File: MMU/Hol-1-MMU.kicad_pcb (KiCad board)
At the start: 2 copper layers, 106.7 x 76.2 mm, 36 parts, among them P1 DATA BUS, P2 ADDRESS PORT, P3 DATA PORT, P4 MMU CONTROL, P5 Power, SW1 HEX_SWITCH, SW2 HEX_SWITCH, SW3 HEX_SWITCH, SW4 HEX_SWITCH, SW5 DPDT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

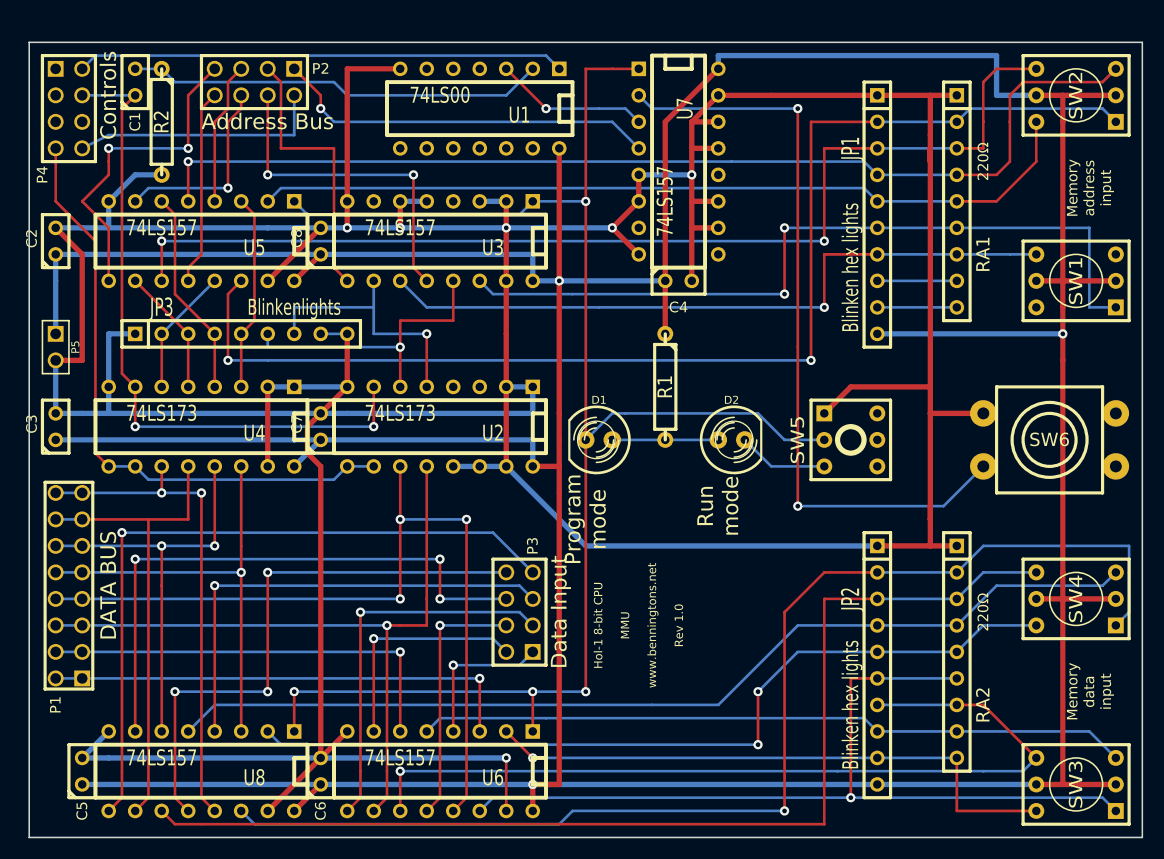
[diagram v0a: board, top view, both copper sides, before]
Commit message: v1.5.10 MMU: better space ICs
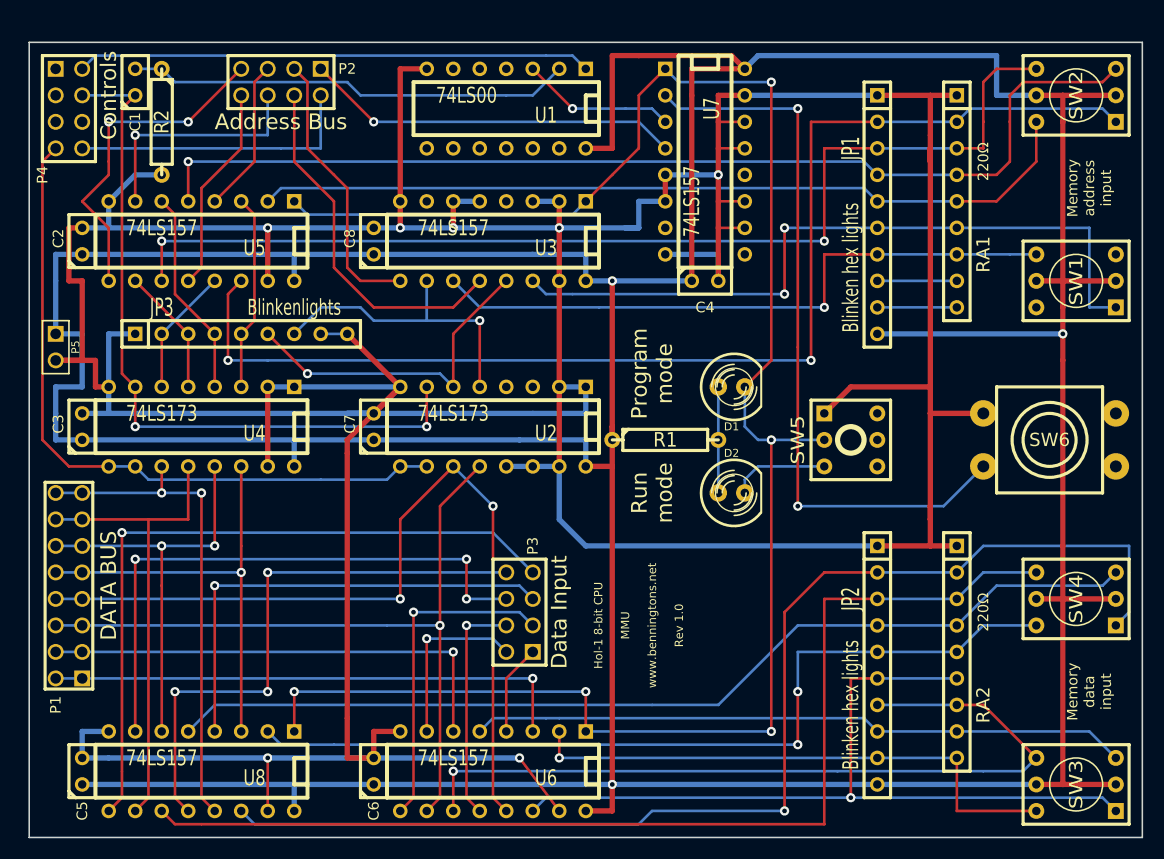
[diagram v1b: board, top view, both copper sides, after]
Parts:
- moved D1 13.7 mm to (171.4, 96.5), turned to 0 degrees
- moved D2 5.08 mm to (171.4, 106.7)
- moved U2 5.08 mm to (148.6, 100.3)
- moved U3 5.08 mm to (148.6, 82.5)
- moved U6 5.08 mm to (148.6, 133.3)
- moved R1 5.08 mm to (165.1, 101.6), turned to 0 degrees
- moved C6 5.08 mm to (137.2, 133.3)
- moved C7 5.08 mm to (137.2, 100.3)
- moved C8 5.08 mm to (137.2, 82.5)
- moved U1 2.54 mm to (149.9, 69.8)
- moved P2 2.54 mm to (128.3, 67.3)
- moved C2 2.54 mm to (109.2, 82.5)
- moved C3 2.54 mm to (109.2, 100.3)
- moved C4 2.54 mm to (168.9, 86.4)
- moved U7 2.54 mm to (168.9, 74.9)
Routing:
- net +5V: track 465.0 -> 492.5 mm
- net GND: track 506.8 -> 534.2 mm, vias 6 -> 7
- net /PROG: track 154.3 -> 179.0 mm, vias 6 -> 7
- net /IN-D: track 59.0 -> 67.4 mm
- net N-0000010: track 14.5 -> 8.67 mm, vias 1 -> 0
- net N-0000046: track 40.6 -> 45.7 mm
- net N-0000045: track 45.7 -> 50.8 mm
- net N-0000040: track 75.5 -> 70.4 mm
- net N-0000021: track 82.6 -> 77.6 mm
- net N-0000011: track 22.1 -> 17.0 mm
- net /CLK: track 64.6 -> 69.6 mm
- net N-0000041: track 67.1 -> 62.0 mm
- net N-0000020: track 83.6 -> 78.5 mm
- net N-0000022: track 68.1 -> 63.1 mm
- net N-0000013: track 36.6 -> 31.5 mm
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
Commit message: v1.5.11 MMU: accommodate larger IDC headers
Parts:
- P1: footprint pin_array_8x2 -> IDC_head_8x2
- P2, P3, P4: footprint pin_array_4x2 -> IDC_head_4x2
- moved C3 3.59 mm to (111.8, 97.8)
- moved C2 2.54 mm to (111.8, 82.5)
- moved C5 2.54 mm to (111.8, 133.3)
- moved JP3 2.54 mm to (127.0, 91.4)
- moved U4 2.54 mm to (123.2, 100.3)
- moved U5 2.54 mm to (123.2, 82.5)
- moved U8 2.54 mm to (123.2, 133.3)
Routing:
- net GND: track 534.2 -> 517.5 mm
- net +5V: track 492.5 -> 480.5 mm
- net N-0000047: track 117.1 -> 109.8 mm, vias 2 -> 1
- net /PROG: track 179.0 -> 174.7 mm
- net N-000006: track 22.9 -> 18.8 mm
- net N-000005: track 32.1 -> 29.3 mm
- net N-0000049: track 101.2 -> 98.6 mm
- net N-0000042: track 46.2 -> 48.8 mm, vias 0 -> 1
- net N-0000056: track 55.1 -> 52.6 mm
- net N-0000053: track 55.9 -> 53.3 mm
- net N-0000044: track 43.2 -> 45.7 mm
- net N-0000054: track 47.5 -> 50.1 mm
- net N-0000052: track 45.0 -> 42.4 mm
- net N-0000048: track 103.4 -> 100.9 mm
- net N-0000039: track 40.6 -> 43.2 mm
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
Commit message: v1.5.12 MMU: accommodate larger JST header
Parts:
- P5: footprint PIN_ARRAY_2X1 -> JST_head_2X1
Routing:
- net +5V: track 480.5 -> 483.4 mm
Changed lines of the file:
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@@
     (links 192)
     (no_connects 0)
-    (area 103.2764 59.706934 210.895001 143.493066)
+    (area 103.733599 58.205512 210.895001 143.493066)
     (thickness 1.6)
     (drawings 13)
@@
   )
   (setup
-    (last_trace_width 0.254)
+    (last_trace_width 0.508)
     (user_trace_width 0.508)
     (trace_clearance 0.254)
@@
     (pcb_text_width 0.3)
     (pcb_text_size 1.5 1.5)
-    (mod_edge_width 0.3048)
+    (mod_edge_width 0.1524)
     (mod_text_size 1 1)
     (mod_text_width 0.15)
@@
     )
   )
-  (module PIN_ARRAY_2X1 (layer F.Cu)
-    (at 106.68 92.71 270)
-    (descr "Connecteurs 2 pins")
-    (tags "CONN DEV")
-    (fp_text reference P5 (at 0 -1.905 270) (layer F.SilkS)
-      (effects (font (size 0.762 0.762) (thickness 0.1524)))
-    )
-    (fp_text value Power (at 0 -1.905 270) (layer F.SilkS) hide
-      (effects (font (size 0.762 0.762) (thickness 0.1524)))
-    )
-    (fp_line (start -2.54 1.27) (end -2.54 -1.27) (layer F.SilkS) (width 0.1524))
-    (fp_line (start -2.54 -1.27) (end 2.54 -1.27) (layer F.SilkS) (width 0.1524))
-    (fp_line (start 2.54 -1.27) (end 2.54 1.27) (layer F.SilkS) (width 0.1524))
-    (fp_line (start 2.54 1.27) (end -2.54 1.27) (layer F.SilkS) (width 0.1524))
-    (pad 1 thru_hole rect (at -1.27 0 270) (size 1.524 1.524) (drill 1.016)
-      (layers *.Cu *.Mask F.SilkS)
-      (net 1 +5V)
-    )
-    (pad 2 thru_hole circle (at 1.27 0 270) (size 1.524 1.524) (drill 1.016)
-      (layers *.Cu *.Mask F.SilkS)
-      (net 8 GND)
-    )
-    (model pin_array/pins_array_2x1.wrl
-      (at (xyz 0 0 0))
-      (scale (xyz 1 1 1))
-      (rotate (xyz 0 0 0))
-    )
-  )
   (module C1 (layer F.Cu)
     (at 111.76 82.55 90)
@@
     )
   )
+  (module JST_head_2X1 (layer F.Cu)
+    (at 106.68 92.71 270)
+    (descr "JST header 2 pins")
+    (tags "CONN JST 2")
+    (fp_text reference P5 (at 0 1.27 270) (layer F.SilkS)
+      (effects (font (size 0.762 0.762) (thickness 0.1524)))
+    )
+    (fp_text value Power (at 0 -1.905 270) (layer F.SilkS)
+      (effects (font (size 0.762 0.762) (thickness 0.1524)))
+    )
+    (fp_line (start 0.635 1.27) (end 2.54 1.27) (layer F.SilkS) (width 0.1524))
+    (fp_line (start -2.54 1.27) (end -0.635 1.27) (layer F.SilkS) (width 0.1524))
+    (fp_line (start -2.54 -1.27) (end -2.54 -2.54) (layer F.SilkS) (width 0.1524))
+    (fp_line (start -2.54 -2.54) (end 2.54 -2.54) (layer F.SilkS) (width 0.1524))
+    (fp_line (start 2.54 -2.54) (end 2.54 -1.27) (layer F.SilkS) (width 0.1524))
+    (fp_line (start -2.54 1.27) (end -2.54 -1.27) (layer F.SilkS) (width 0.1524))
+    (fp_line (start 2.54 -1.27) (end 2.54 1.27) (layer F.SilkS) (width 0.1524))
+    (pad 1 thru_hole rect (at -1.27 0 270) (size 1.524 1.524) (drill 1.016)
+      (layers *.Cu *.Mask F.SilkS)
+      (net 1 +5V)
+    )
+    (pad 2 thru_hole circle (at 1.27 0 270) (size 1.524 1.524) (drill 1.016)
+      (layers *.Cu *.Mask F.SilkS)
+      (net 8 GND)
+    )
+    (model pin_array/pins_array_2x1.wrl
+      (at (xyz 0 0 0))
+      (scale (xyz 1 1 1))
+      (rotate (xyz 0 0 0))
+    )
+  )
   (gr_text "Program\nmode" (at 163.83 95.25 90) (layer F.SilkS)
     (effects (font (size 1.5 1.5) (thickness 0.3)))
@@
   (gr_line (start 104.14 139.7) (end 210.82 139.7) (angle 90) (layer Edge.Cuts) (width 0.15))
   (gr_line (start 104.14 63.5) (end 104.14 139.7) (angle 90) (layer Edge.Cuts) (width 0.15))
+  (segment (start 106.68 91.44) (end 106.68 83.82) (width 0.508) (layer B.Cu) (net 1) (status 400000))
+  (segment (start 106.68 83.82) (end 111.76 83.82) (width 0.508) (layer B.Cu) (net 1) (status 800000))
   (segment (start 111.76 99.06) (end 114.3 101.6) (width 0.508) (layer B.Cu) (net 1))
   (segment (start 114.3 101.6) (end 132.08 101.6) (width 0.508) (layer B.Cu) (net 1))
   (segment (start 111.76 83.82) (end 132.08 83.82) (width 0.508) (layer B.Cu) (net 1))
-  (segment (start 106.68 91.44) (end 111.76 86.36) (width 0.508) (layer B.Cu) (net 1))
-  (segment (start 111.76 86.36) (end 111.76 83.82) (width 0.508) (layer B.Cu) (net 1))
   (segment (start 132.08 86.36) (end 132.08 83.82) (width 0.508) (layer B.Cu) (net 1))
   (segment (start 111.76 99.06) (end 109.22 99.06) (width 0.508) (layer B.Cu) (net 1))

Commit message: v1.5.13 MMU: adjustments during construction
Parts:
- C3: footprint C1 -> C2
- moved C3 1.27 mm to (111.8, 99.1)
- turned SW5 to 90 degrees
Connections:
- SW6 pad 1: GND -> N-0000057
- SW6 pad 2: N-0000057 -> GND
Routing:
- net /PROG: track 174.7 -> 190.2 mm, vias 7 -> 6
- net N-0000057: track 70.7 -> 56.5 mm
- net GND: track 517.5 -> 508.8 mm
- net N-000009: track 9.42 -> 18.1 mm
- net +5V: track 483.4 -> 484.5 mm, vias 3 -> 6
- net /IN-D: track 66.7 -> 67.4 mm

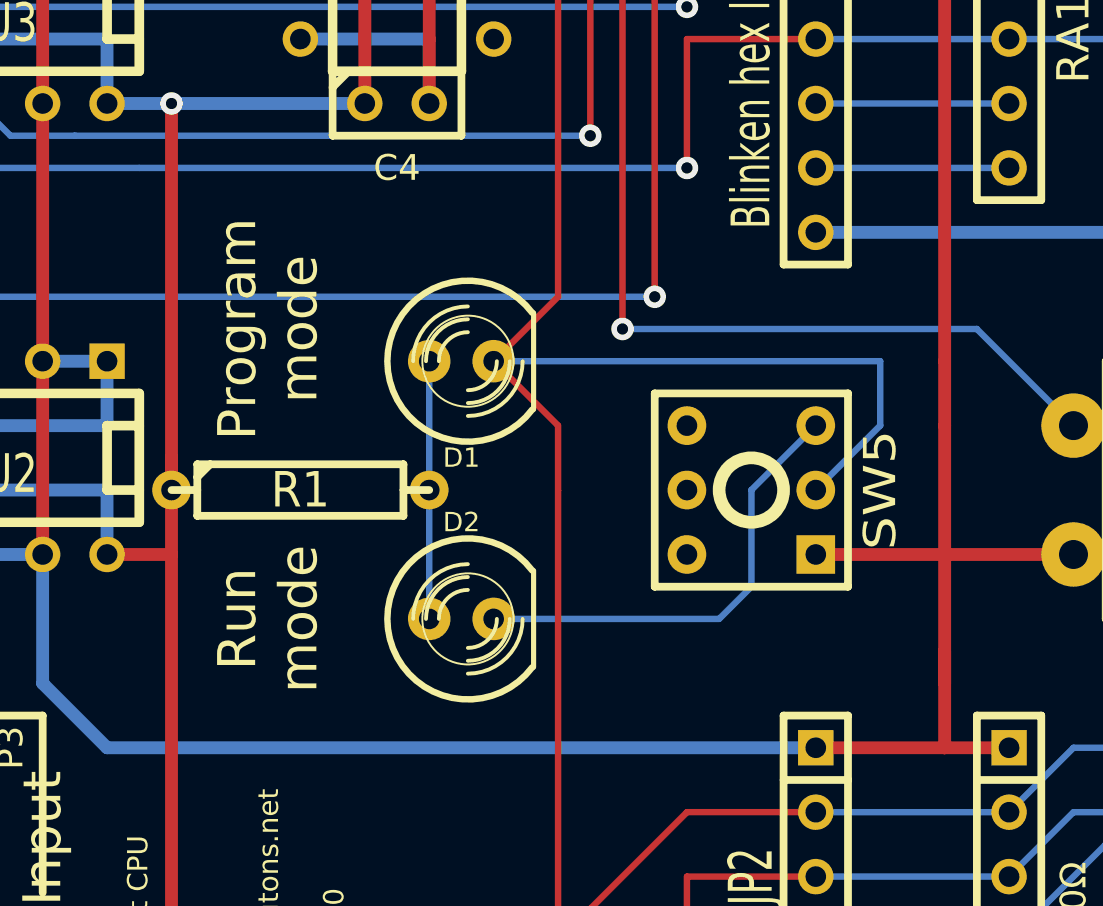
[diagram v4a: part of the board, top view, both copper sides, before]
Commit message: v1.5.16 MMU: don't share a resistor between program and run LEDs
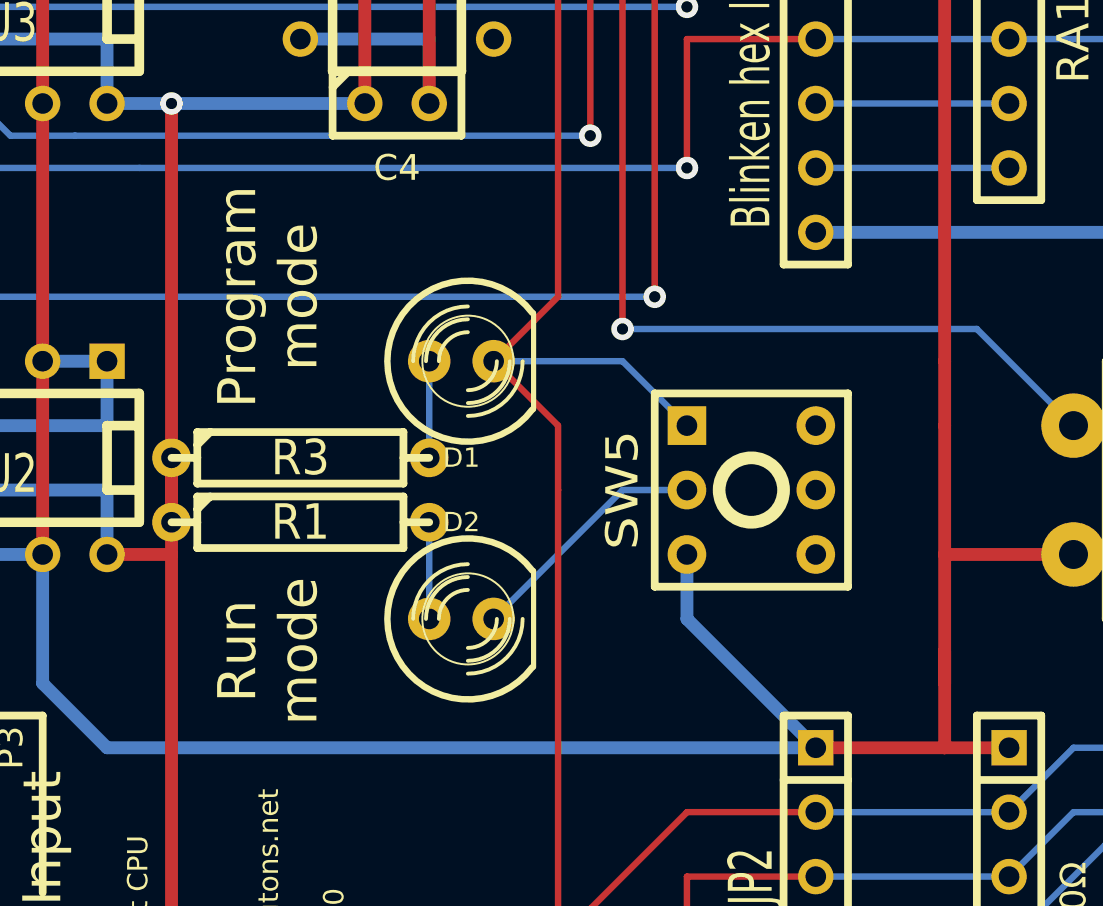
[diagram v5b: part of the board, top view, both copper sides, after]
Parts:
- added R3: 220Ω, R4, F.Cu at (165.1, 100.3)
- moved R1 1.27 mm to (165.1, 102.9)
- turned SW5 to 270 degrees
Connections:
- D1 pad 1: N-0000063 -> N-000007
- D2 pad 1: N-0000063 -> N-000008
- D2 pad 2: N-000009 -> N-000005
- R1 pad 2: N-0000063 -> N-000008
- SW5 pad 1: GND -> /PROG
- SW5 pad 2: /PROG -> N-000005
- SW5 pad 3: N-000009 -> GND
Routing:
- net N-000009: track 18.1 -> 0.00 mm
- net /PROG: track 190.2 -> 177.5 mm
- net N-0000063: track 10.2 -> 0.00 mm
- net N-000005: track 0.00 -> 9.72 mm
- net GND: track 508.8 -> 513.4 mm
- net N-000008: track 0.00 -> 3.81 mm
- net N-000007: track 0.00 -> 3.81 mm
- net +5V: track 484.5 -> 485.8 mm

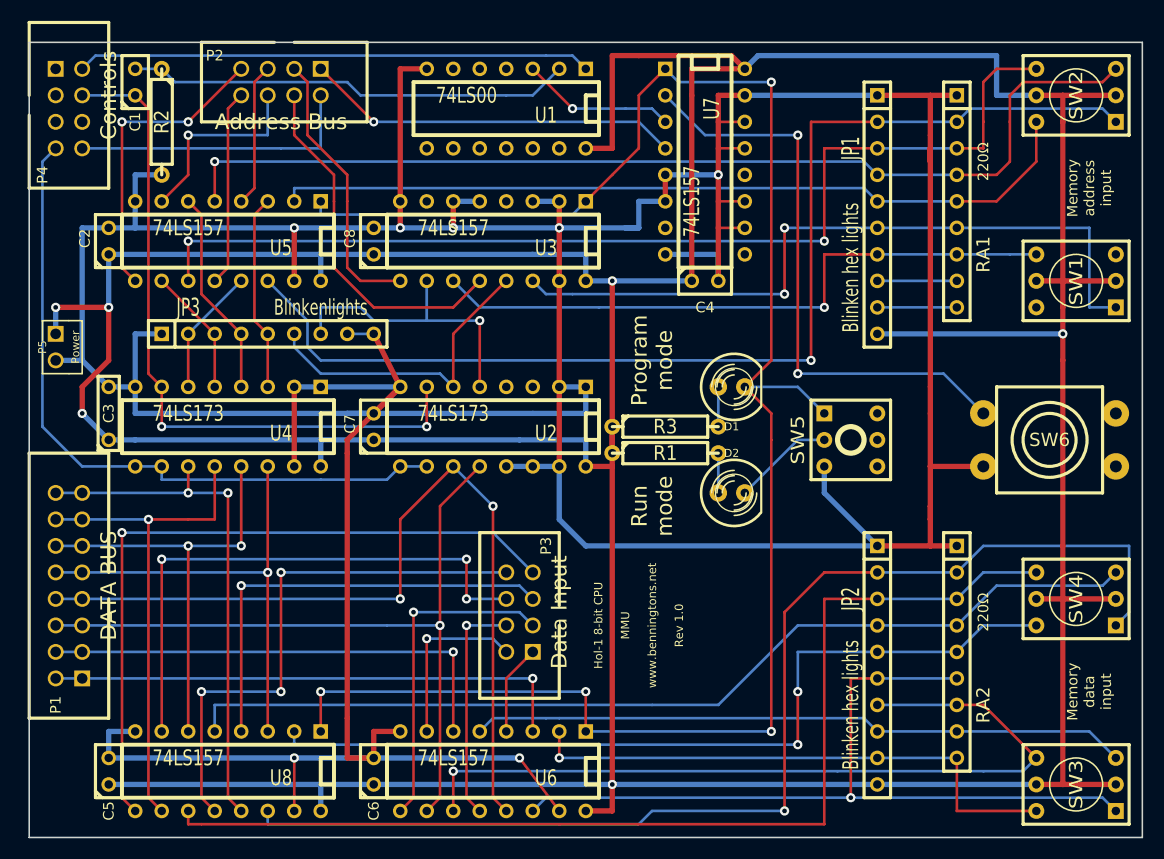
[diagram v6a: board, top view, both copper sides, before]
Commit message: 1.5.21 upgraded to KiCad 6.0
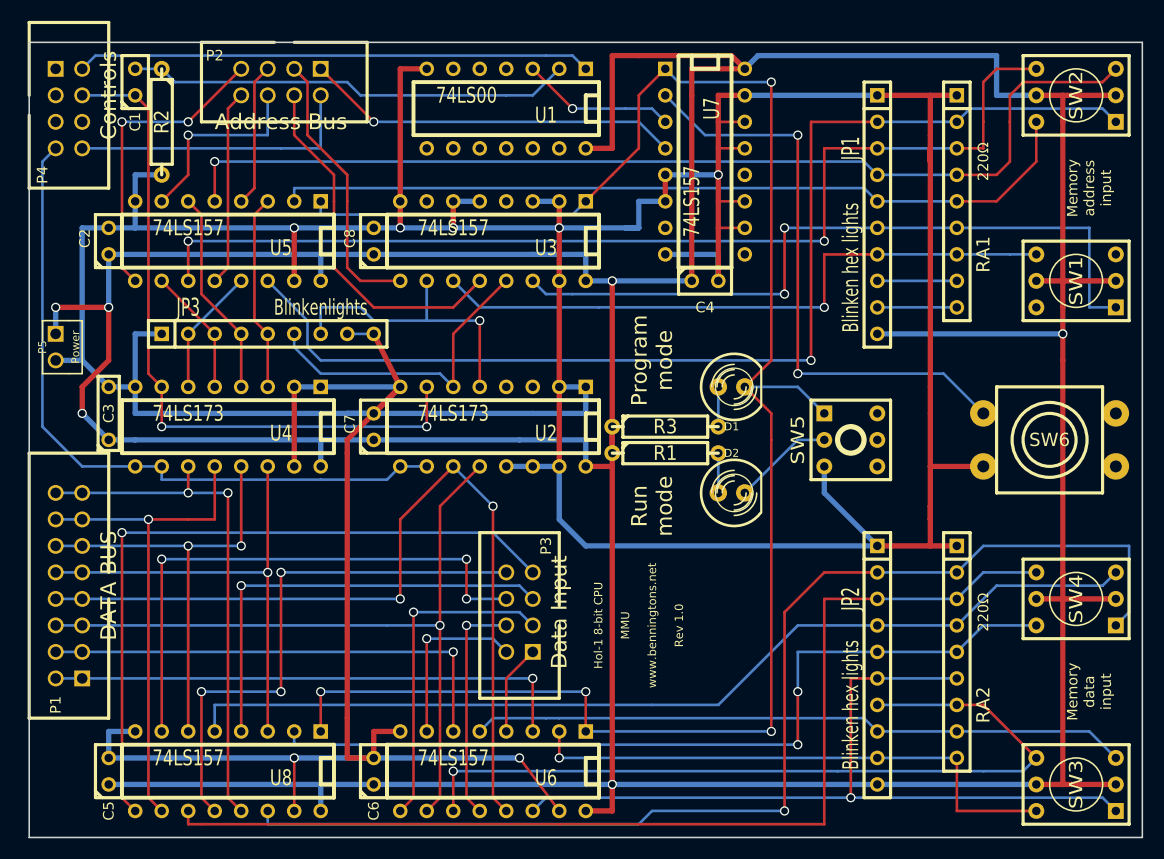
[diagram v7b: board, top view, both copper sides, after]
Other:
- net class Default removed
